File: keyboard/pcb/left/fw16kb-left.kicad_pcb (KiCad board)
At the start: 2 copper layers, 0 parts

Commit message: keyboard left PCB: outline + 2-layer 1.2 mm stackup, 57 footprints from the schematic, keys/diodes/U1/J1 from positions-b.csv (diodes on B.Cu), link parts in the controller zone; lesson
Co-Authored-By: Claude Opus 5.5 (1M context) <noreply@anthropic.com>
Claude-Session: https://claude.ai/code/session_019QA2U79cSHCaAaMe6Km575
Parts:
- added D1: 1N4148W, Diode_SMD:D_SOD-123, B.Cu at (0.00, -29.3)
- added D10: 1N4148W, Diode_SMD:D_SOD-123, B.Cu at (54.0, -21.3)
- added D11: 1N4148W, Diode_SMD:D_SOD-123, B.Cu at (72.0, -17.3)
- added D12: 1N4148W, Diode_SMD:D_SOD-123, B.Cu at (90.0, -15.3)
- added D13: 1N4148W, Diode_SMD:D_SOD-123, B.Cu at (0.00, 4.70)
- added D14: 1N4148W, Diode_SMD:D_SOD-123, B.Cu at (18.0, 4.70)
- added D15: 1N4148W, Diode_SMD:D_SOD-123, B.Cu at (36.0, -1.30)
- added D16: 1N4148W, Diode_SMD:D_SOD-123, B.Cu at (54.0, -4.30)
- added D17: 1N4148W, Diode_SMD:D_SOD-123, B.Cu at (72.0, -0.30)
- added D18: 1N4148W, Diode_SMD:D_SOD-123, B.Cu at (90.0, 1.70)
- added D19: 1N4148W, Diode_SMD:D_SOD-123, B.Cu at (63.0, 19.7)
- added D2: 1N4148W, Diode_SMD:D_SOD-123, B.Cu at (18.0, -29.3)
- added D20: 1N4148W, Diode_SMD:D_SOD-123, B.Cu at (81.6, 21.7)
- added D21: 1N4148W, Diode_SMD:D_SOD-123, B.Cu at (99.4, 27.4)
- added D22: B5819W, Diode_SMD:D_SOD-123, F.Cu at (105.0, -20.5)
- added D3: 1N4148W, Diode_SMD:D_SOD-123, B.Cu at (36.0, -35.3)
- added D4: 1N4148W, Diode_SMD:D_SOD-123, B.Cu at (54.0, -38.3)
- added D5: 1N4148W, Diode_SMD:D_SOD-123, B.Cu at (72.0, -34.3)
- added D6: 1N4148W, Diode_SMD:D_SOD-123, B.Cu at (90.0, -32.3)
- added D7: 1N4148W, Diode_SMD:D_SOD-123, B.Cu at (0.00, -12.3)
- added D8: 1N4148W, Diode_SMD:D_SOD-123, B.Cu at (18.0, -12.3)
- added D9: 1N4148W, Diode_SMD:D_SOD-123, B.Cu at (36.0, -18.3)
- added F1: PTC 200mA hold, Fuse:Fuse_0805_2012Metric, F.Cu at (108.5, -16.0)
- added H1: M2, MountingHole:MountingHole_2.2mm_M2, F.Cu at (7.45, 199.7)
- added H2: M2, MountingHole:MountingHole_2.2mm_M2, F.Cu at (7.45, 209.6)
- added H3: M2, MountingHole:MountingHole_2.2mm_M2, F.Cu at (7.45, 219.4)
- added H4: M2, MountingHole:MountingHole_2.2mm_M2, F.Cu at (7.45, 229.3)
- added J1: HRO TYPE-C-31-M-12, Connector_USB:USB_C_Receptacle_HRO_TYPE-C-31-M-12, F.Cu at (122.0, -14.0)
- added Q1: AO3401A, Package_TO_SOT_SMD:SOT-23, F.Cu at (105.0, -16.0)
- added Q2: AO3401A, Package_TO_SOT_SMD:SOT-23, F.Cu at (105.0, -11.0)
- added R1: 56k, Resistor_SMD:R_0805_2012Metric, F.Cu at (101.5, -16.0)
- added R2: 56k, Resistor_SMD:R_0805_2012Metric, F.Cu at (101.5, -11.0)
- added R3: 330, Resistor_SMD:R_0805_2012Metric, F.Cu at (108.5, -11.0)
- added R4: 10k, Resistor_SMD:R_0805_2012Metric, F.Cu at (112.0, -16.0)
- added SW1: Choc v1, fw16kb:Choc_v1_Hotswap, F.Cu at (0.00, -34.0)
- added SW10: Choc v1, fw16kb:Choc_v1_Hotswap, F.Cu at (54.0, -26.0)
- added SW11: Choc v1, fw16kb:Choc_v1_Hotswap, F.Cu at (72.0, -22.0)
- added SW12: Choc v1, fw16kb:Choc_v1_Hotswap, F.Cu at (90.0, -20.0)
- added SW13: Choc v1, fw16kb:Choc_v1_Hotswap, F.Cu at (0.00, 0.00)
- added SW14: Choc v1, fw16kb:Choc_v1_Hotswap, F.Cu at (18.0, 0.00)
- added SW15: Choc v1, fw16kb:Choc_v1_Hotswap, F.Cu at (36.0, -6.00)
- added SW16: Choc v1, fw16kb:Choc_v1_Hotswap, F.Cu at (54.0, -9.00)
- added SW17: Choc v1, fw16kb:Choc_v1_Hotswap, F.Cu at (72.0, -5.00)
- added SW18: Choc v1, fw16kb:Choc_v1_Hotswap, F.Cu at (90.0, -3.00)
- added SW19: Choc v1, fw16kb:Choc_v1_Hotswap, F.Cu at (63.0, 15.0)
- added SW2: Choc v1, fw16kb:Choc_v1_Hotswap, F.Cu at (18.0, -34.0)
- added SW20: Choc v1, fw16kb:Choc_v1_Hotswap, F.Cu at (82.6, 17.1)
- added SW21: Choc v1, fw16kb:Choc_v1_Hotswap, F.Cu at (101.3, 23.1)
- added SW3: Choc v1, fw16kb:Choc_v1_Hotswap, F.Cu at (36.0, -40.0)
- added SW4: Choc v1, fw16kb:Choc_v1_Hotswap, F.Cu at (54.0, -43.0)
- added SW5: Choc v1, fw16kb:Choc_v1_Hotswap, F.Cu at (72.0, -39.0)
- added SW6: Choc v1, fw16kb:Choc_v1_Hotswap, F.Cu at (90.0, -37.0)
- added SW7: Choc v1, fw16kb:Choc_v1_Hotswap, F.Cu at (0.00, -17.0)
- added SW8: Choc v1, fw16kb:Choc_v1_Hotswap, F.Cu at (18.0, -17.0)
- added SW9: Choc v1, fw16kb:Choc_v1_Hotswap, F.Cu at (36.0, -23.0)
- added U1: RP2040-Zero, fw16kb:RP2040-Zero_Castellated, F.Cu at (110.0, -34.8)
- added U2: USBLC6-2SC6, Package_TO_SOT_SMD:SOT-23-6, F.Cu at (112.0, -11.0)
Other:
- board outline added: 132 x 88.1 mm

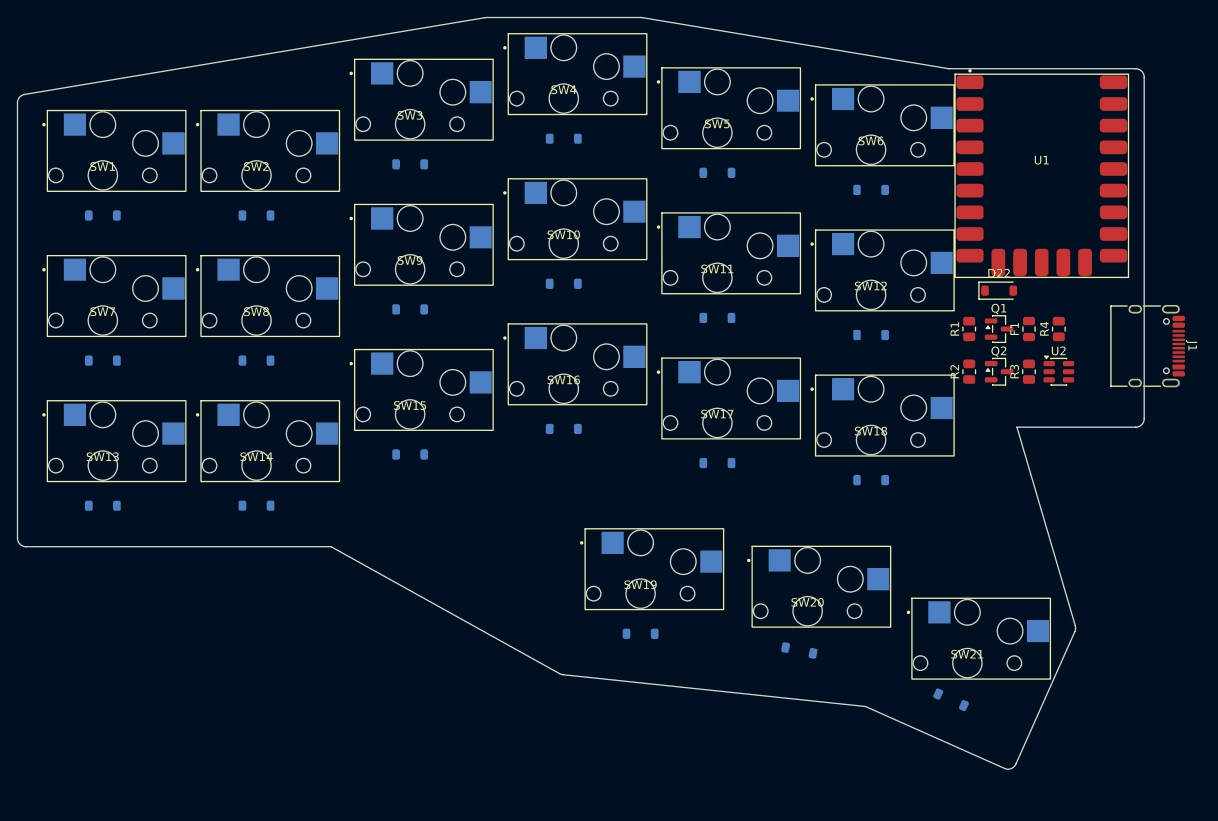
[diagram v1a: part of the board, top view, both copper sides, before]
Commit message: keyboard left PCB: Choc footprints refreshed, SW20/SW21 at -12/-24; both boards placed; chat log
Co-Authored-By: Claude Opus 5.5 (1M context) <noreply@anthropic.com>
Claude-Session: https://claude.ai/code/session_019QA2U79cSHCaAaMe6Km575
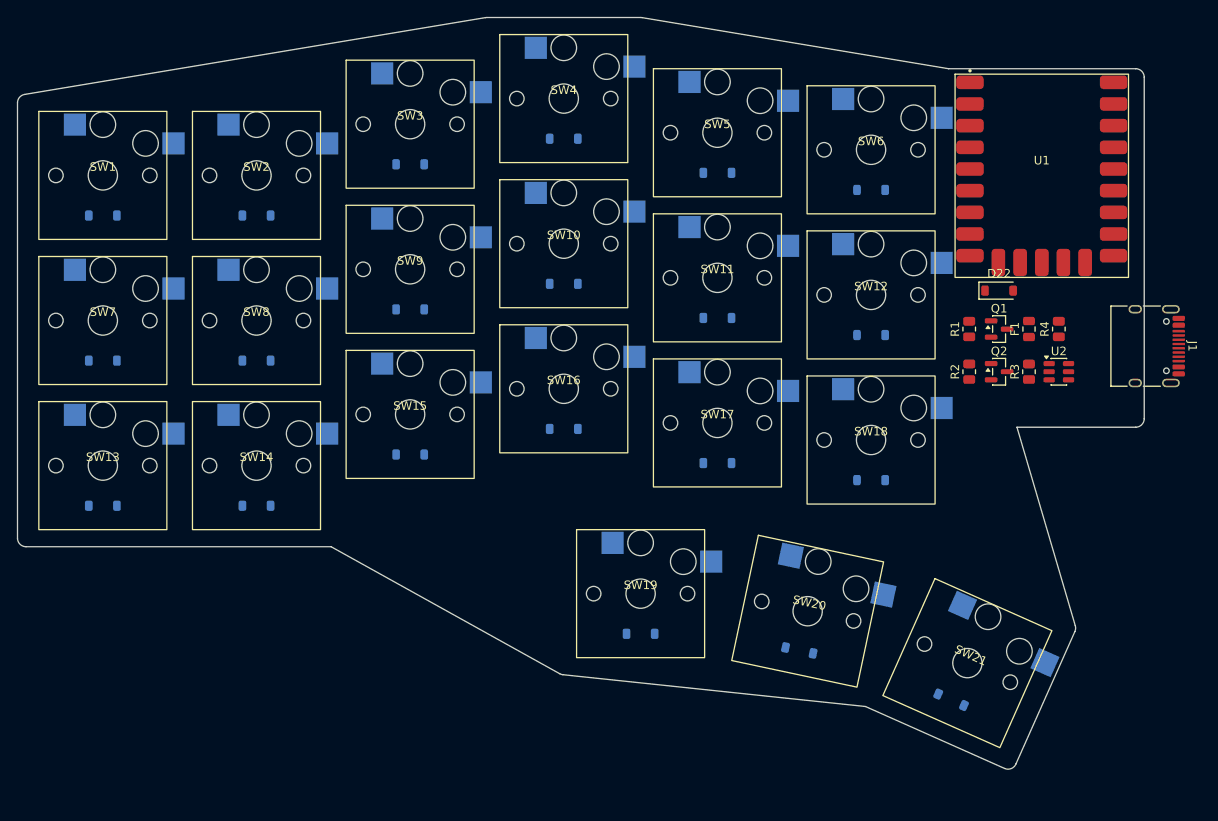
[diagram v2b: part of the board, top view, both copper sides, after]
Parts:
- turned SW20 to -12 degrees
- turned SW21 to -24 degrees

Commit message: keyboard left PCB: M2 mounting holes H1-H4 (top pocket, bottom pocket, thumb gap, controller corner)
Co-Authored-By: Claude Opus 5.5 (1M context) <noreply@anthropic.com>
Claude-Session: https://claude.ai/code/session_019QA2U79cSHCaAaMe6Km575
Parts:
- moved H4 253.6 mm to (102.0, -6.00)
- moved H1 245.8 mm to (25.5, -45.5)
- moved H3 221.9 mm to (62.5, 4.50)
- moved H2 205.3 mm to (30.0, 5.50)
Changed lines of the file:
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@@
 	(footprint "MountingHole:MountingHole_2.2mm_M2"
 		(layer "F.Cu")
-		(at 7.45 229.35)
+		(at 102 -6)
 		(property "Reference" "H4"
 			(at 0 -3.15 0)
@@
 	(footprint "MountingHole:MountingHole_2.2mm_M2"
 		(layer "F.Cu")
-		(at 7.45 219.45)
+		(at 62.5 4.5)
 		(property "Reference" "H3"
 			(at 0 -3.15 0)
@@
 	(footprint "MountingHole:MountingHole_2.2mm_M2"
 		(layer "F.Cu")
-		(at 7.45 209.55)
+		(at 30 5.5)
 		(property "Reference" "H2"
 			(at 0 -3.15 0)
@@
 	(footprint "MountingHole:MountingHole_2.2mm_M2"
 		(layer "F.Cu")
-		(at 7.45 199.65)
+		(at 25.5 -45.5)
 		(property "Reference" "H1"
 			(at 0 -3.15 0)

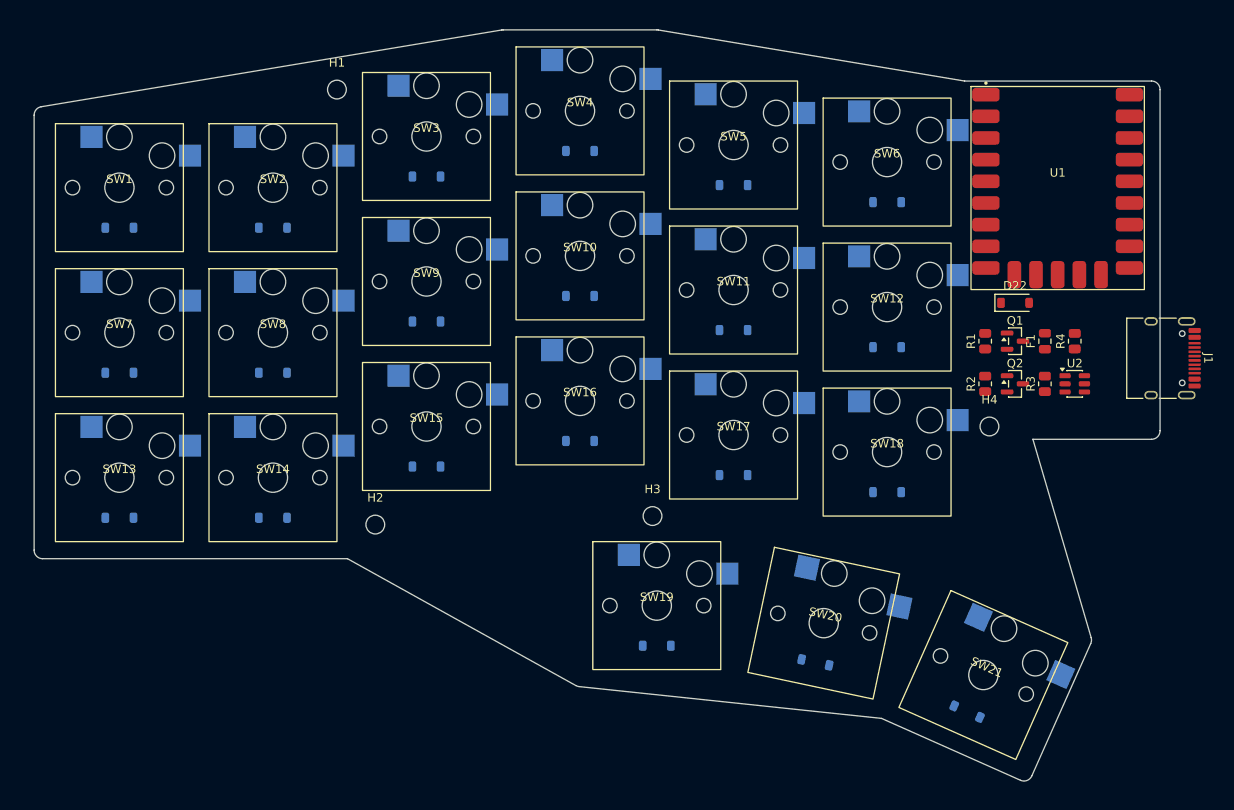
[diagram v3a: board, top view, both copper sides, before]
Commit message: keyboard left PCB: J1 mouth-out (1 mm overhang), link parts 2.5 mm inward; routed (freerouting + C2/D21 by hand), GND pours both layers; DRC: only SW21 pad 0.42 mm from edge (accepted)
Co-Authored-By: Claude Opus 5.5 (1M context) <noreply@anthropic.com>
Claude-Session: https://claude.ai/code/session_019QA2U79cSHCaAaMe6Km575
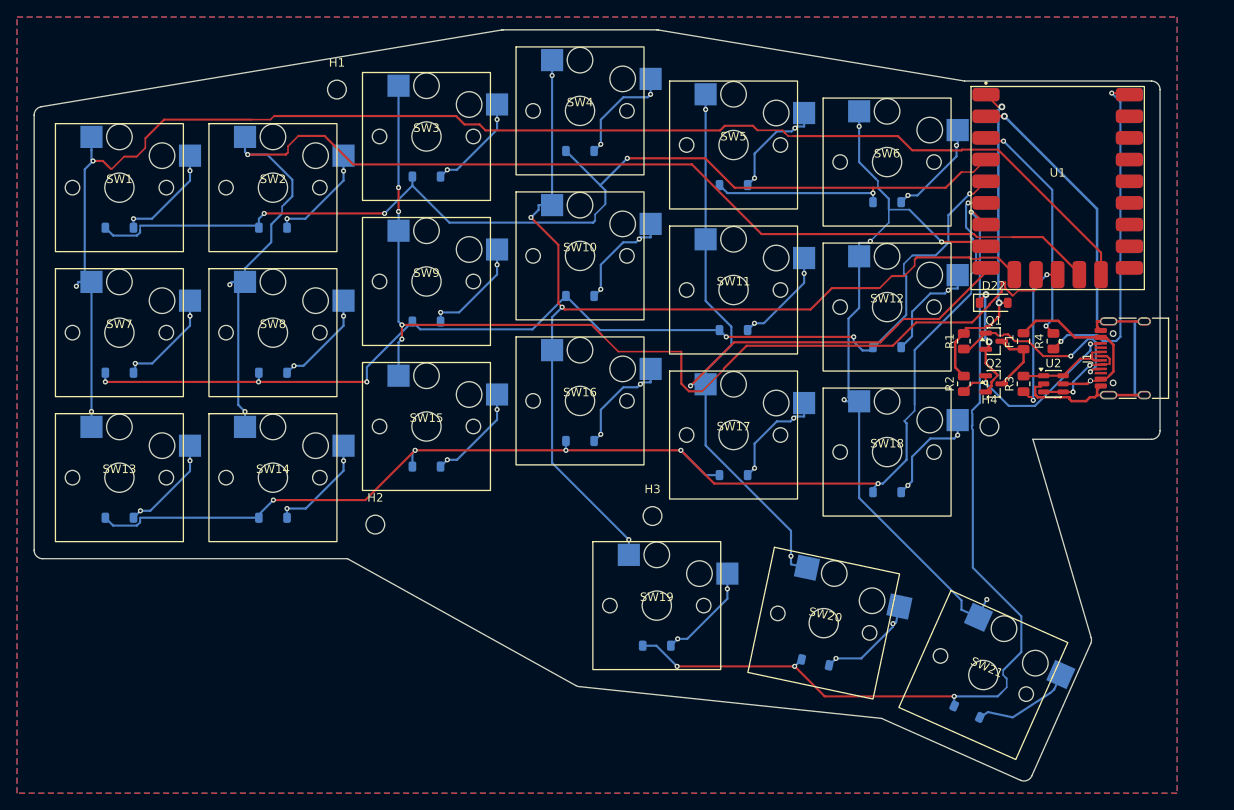
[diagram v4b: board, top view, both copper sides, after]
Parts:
- moved J1 2.90 mm to (119.1, -14.0), turned to 90 degrees
- moved D22 2.50 mm to (102.5, -20.5)
- moved F1 2.50 mm to (106.0, -16.0)
- moved Q1 2.50 mm to (102.5, -16.0)
- moved Q2 2.50 mm to (102.5, -11.0)
- moved R1 2.50 mm to (99.0, -16.0)
- moved R2 2.50 mm to (99.0, -11.0)
- moved R3 2.50 mm to (106.0, -11.0)
- moved R4 2.50 mm to (109.5, -16.0)
- moved U2 2.50 mm to (109.5, -11.0)
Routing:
- net /C0: track 0.00 -> 168.2 mm, vias 0 -> 3
- net /C1: track 0.00 -> 147.9 mm, vias 0 -> 3
- net /R2: track 0.00 -> 147.9 mm, vias 0 -> 6
- net /R0: track 0.00 -> 144.4 mm, vias 0 -> 4
- net /R1: track 0.00 -> 128.3 mm, vias 0 -> 6
- net /C2: track 0.00 -> 123.2 mm, vias 0 -> 4
- net /C3: track 0.00 -> 122.8 mm, vias 0 -> 4
- net /R3: track 0.00 -> 110.2 mm, vias 0 -> 4
- net /C4: track 0.00 -> 106.2 mm, vias 0 -> 3
- net /C5: track 0.00 -> 87.1 mm, vias 0 -> 5
- net /GND: track 0.00 -> 66.5 mm, vias 0 -> 1
- net /HAND: track 0.00 -> 40.2 mm, vias 0 -> 2
- net /+5V: track 0.00 -> 39.3 mm, vias 0 -> 2
- net /+3V3: track 0.00 -> 27.8 mm, vias 0 -> 2
- net /LINK_CC1: track 0.00 -> 23.5 mm, vias 0 -> 2
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- added copper zone on B.Cu, net /GND
- added copper zone on F.Cu, net /GND

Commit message: keyboard left PCB: single-layer vias removed (KiCad cleanup), first stub segments deleted; 0 unrouted
Co-Authored-By: Claude Opus 5.5 (1M context) <noreply@anthropic.com>
Claude-Session: https://claude.ai/code/session_019QA2U79cSHCaAaMe6Km575
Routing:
- net /C5: track 87.1 -> 86.7 mm, vias 5 -> 1
- net /C1: track 147.9 -> 147.6 mm, vias 3 -> 1
- net /C0: track 168.2 -> 167.9 mm, vias 3 -> 1
- net Net-(D9-A): vias 2 -> 0
- net Net-(D8-A): vias 2 -> 0
- net Net-(D7-A): vias 2 -> 0
- net Net-(D6-A): vias 2 -> 0
- net Net-(D5-A): vias 2 -> 0
- net Net-(D4-A): vias 2 -> 0
- net Net-(D3-A): vias 2 -> 0
- net Net-(D20-A): vias 2 -> 0
- net Net-(D2-A): vias 2 -> 0
- net Net-(D19-A): vias 2 -> 0
- net Net-(D18-A): vias 2 -> 0
- net Net-(D17-A): vias 2 -> 0
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
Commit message: keyboard left PCB: dangling stubs removed (KiCad cleanup); both boards routed, DRC clean apart from the accepted SW21 edge pad
Co-Authored-By: Claude Opus 5.5 (1M context) <noreply@anthropic.com>
Claude-Session: https://claude.ai/code/session_019QA2U79cSHCaAaMe6Km575
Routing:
- net /C5: track 86.7 -> 83.8 mm
- net /C0: track 167.9 -> 166.8 mm
- net /C1: track 147.6 -> 146.7 mm
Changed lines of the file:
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@@
-	)
-	(segment
-		(start 100.7142 16.3703)
-		(end 101.6017 14.377)
-		(width 0.25)
-		(layer "B.Cu")
-		(net "/C5")
 	)
 	(segment
@@
 		(start 85.4805 -18.6479)
 		(end 86.725 -19.8924)
-		(width 0.25)
-		(layer "B.Cu")
-		(net "/C5")
-	)
-	(segment
-		(start 85.9367 -8.95)
-		(end 85.1483 -8.95)
 		(width 0.25)
 		(layer "B.Cu")
@@
 	)
 	(segment
-		(start 13.1483 -22.8285)
-		(end 13.1483 -22.95)
-		(width 0.25)
-		(layer "B.Cu")
-		(net "/C1")
-	)
-	(segment
-		(start 13.9367 -22.95)
-		(end 13.1483 -22.95)
-		(width 0.25)
-		(layer "B.Cu")
-		(net "/C1")
-	)
-	(segment
 		(start 19.0748 -30.9704)
 		(end 17.7998 -29.6954)
@@
 		(width 0.25)
 		(layer "B.Cu")
-		(net "/C0")
-	)
-	(segment
-		(start -4.0633 -22.95)
-		(end -4.8517 -22.95)
-		(width 0.25)
-		(layer "B.Cu")
-		(net "/C0")
-	)
-	(segment
-		(start -4.8517 -22.6347)
-		(end -4.8517 -22.95)
-		(width 0.25)
-		(layer "B.Cu")
